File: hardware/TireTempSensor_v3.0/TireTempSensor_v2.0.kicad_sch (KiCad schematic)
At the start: 17 parts, among them J2 Main connector, J3 FTSH-107-01-L-D-K, U1 STM32G0C1KCTxN, Y1 ATX-11-F-32.000MHZ-F05-T

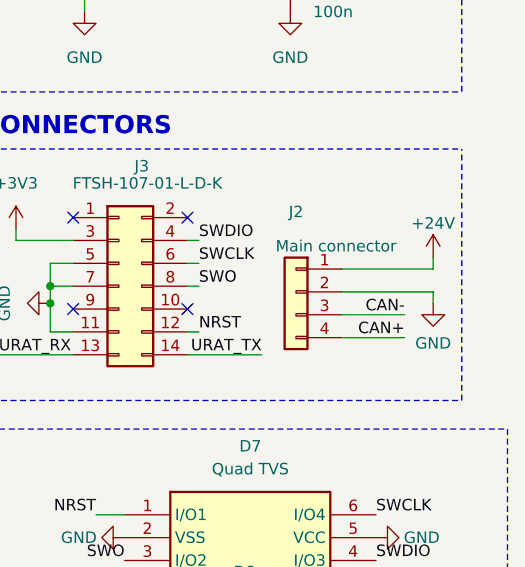
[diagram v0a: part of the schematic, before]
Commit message: Z wielkim bólem przesunięte złącze aby poprawić routing cana
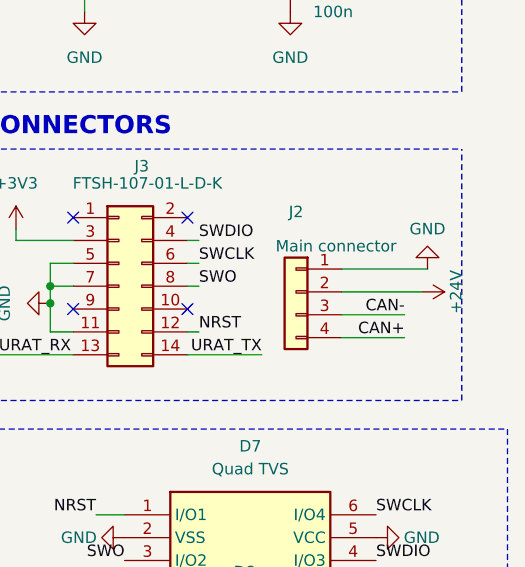
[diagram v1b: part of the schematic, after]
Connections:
- net +24V: now also J2.2 (Pin_2); no longer J2.1 (Pin_1)
- net GND: now also J2.1 (Pin_1); no longer J2.2 (Pin_2)
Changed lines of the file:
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@@
+		)
+	)
+	(wire
+		(pts
+			(xy 263.525 107.315) (xy 273.05 107.315)
+		)
+		(stroke
+			(width 0)
+			(type default)
 		)
 	)
@@
 	(wire
 		(pts
-			(xy 263.525 109.855) (xy 273.685 109.855)
-		)
-		(stroke
-			(width 0)
-			(type default)
-		)
-	)
-	(wire
-		(pts
 			(xy 106.68 130.175) (xy 96.52 130.175)
 		)
@@
 	(wire
 		(pts
-			(xy 273.685 109.855) (xy 273.685 111.125)
-		)
-		(stroke
-			(width 0)
-			(type default)
-		)
-	)
-	(wire
-		(pts
 			(xy 37.465 39.37) (xy 45.085 39.37)
 		)
@@
 	(wire
 		(pts
-			(xy 273.685 107.315) (xy 273.685 106.045)
-		)
-		(stroke
-			(width 0)
-			(type default)
-		)
-	)
-	(wire
-		(pts
 			(xy 45.085 39.37) (xy 52.705 39.37)
 		)
@@
 	(wire
 		(pts
-			(xy 263.525 107.315) (xy 273.685 107.315)
-		)
-		(stroke
-			(width 0)
-			(type default)
-		)
-	)
-	(wire
-		(pts
 			(xy 96.52 120.015) (xy 106.68 120.015)
 		)
@@
 		(pts
 			(xy 50.165 142.875) (xy 58.42 142.875)
+		)
+		(stroke
+			(width 0)
+			(type default)
+		)
+	)
+	(wire
+		(pts
+			(xy 272.415 109.855) (xy 263.525 109.855)
 		)
 		(stroke
@@
 	(symbol
 		(lib_id "power:GND")
-		(at 273.685 111.125 0)
-		(mirror y)
+		(at 273.05 107.315 0)
+		(mirror x)
 		(unit 1)
 		(exclude_from_sim no)
@@
 		(dnp no)
 		(property "Reference" "#PWR0103"
-			(at 273.685 117.475 0)
+			(at 273.05 100.965 0)
 			(effects
 				(font
@@
 		)
 		(property "Value" "GND"
-			(at 273.685 115.57 0)
+			(at 273.05 102.87 0)
 			(effects
 				(font
@@
 		)
 		(property "Footprint" ""
-			(at 273.685 111.125 0)
+			(at 273.05 107.315 0)
 			(effects
 				(font
@@
 		)
 		(property "Datasheet" ""
-			(at 273.685 111.125 0)
+			(at 273.05 107.315 0)
 			(effects
 				(font
@@
 		)
 		(property "Description" ""
-			(at 273.685 111.125 0)
+			(at 273.05 107.315 0)
 			(effects
 				(font
@@
 	(symbol
 		(lib_id "power:+24V")
-		(at 273.685 106.045 0)
+		(at 272.415 109.855 270)
 		(unit 1)
 		(exclude_from_sim no)
@@
 		(dnp no)
 		(property "Reference" "#PWR0107"
-			(at 273.685 109.855 0)
+			(at 268.605 109.855 0)
 			(effects
 				(font
@@
 		)
 		(property "Value" "+24V"
-			(at 273.685 102.235 0)
+			(at 276.225 109.855 0)
 			(effects
 				(font
@@
 		)
 		(property "Footprint" ""
-			(at 273.685 106.045 0)
+			(at 272.415 109.855 0)
 			(effects
 				(font
@@
 		)
 		(property "Datasheet" ""
-			(at 273.685 106.045 0)
+			(at 272.415 109.855 0)
 			(effects
 				(font
@@
 		)
 		(property "Description" ""
-			(at 273.685 106.045 0)
-			(effects
-				(font
+			(at 272.415 109.855 0)
+			(effects
+				(font

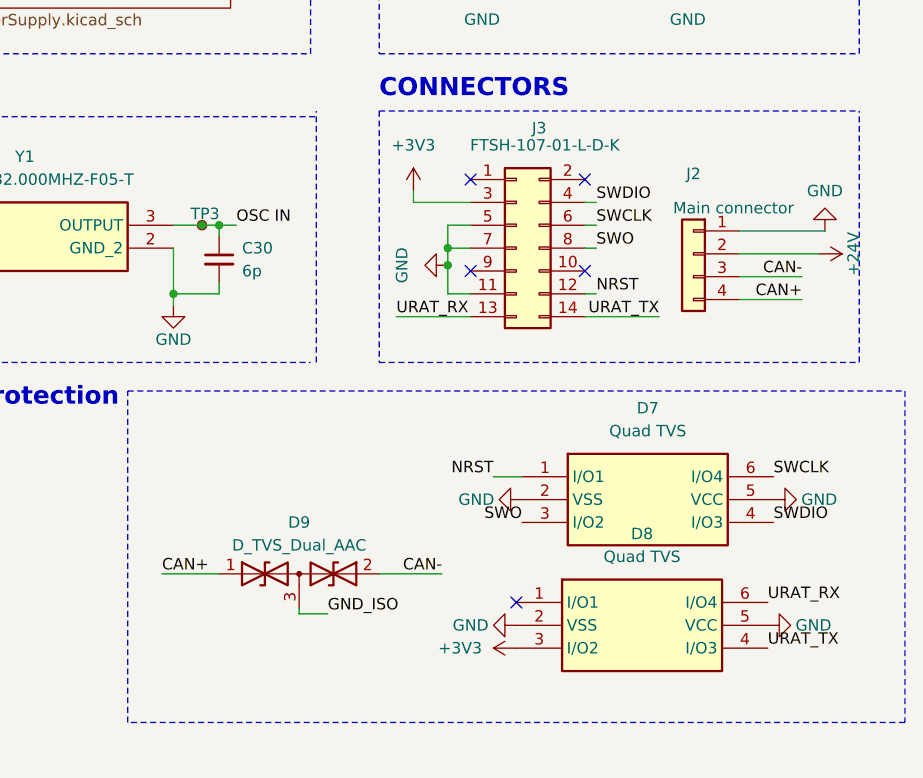
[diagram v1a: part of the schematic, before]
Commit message: Added aditional emi prevention measures
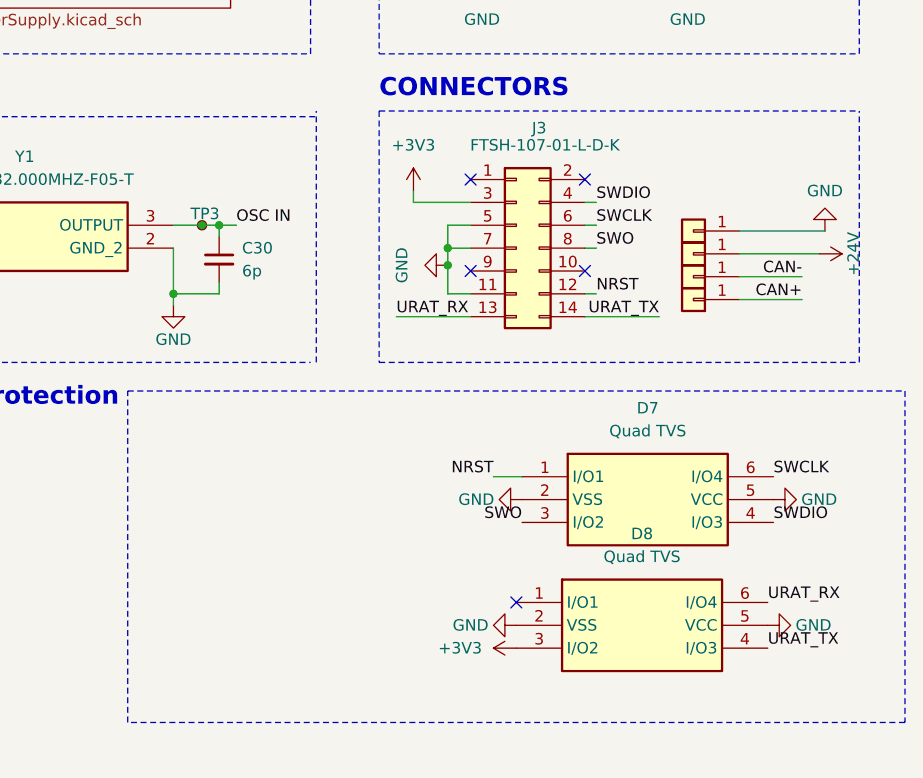
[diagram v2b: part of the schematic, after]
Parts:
- removed D9: D_TVS_Dual_AAC, Package_TO_SOT_SMD:SOT-23_Handsoldering, symbol Device:D_TVS_Dual_AAC
- removed J2: Main connector, footprint:M80-51004YY, symbol Connector_Generic:Conn_01x04
- added J1, J2, J4, J5: Conn_01x01, Connector_Wire:SolderWire-0.1sqmm_1x01_D0.4mm_OD1mm_Relief, symbol Connector_Generic:Conn_01x01
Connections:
- net +24V: now also J2.1 (Pin_1)
- net CAN+: now also J5.1 (Pin_1)
- net CAN-: now also J4.1 (Pin_1)
- net GND: now also J1.1 (Pin_1)
